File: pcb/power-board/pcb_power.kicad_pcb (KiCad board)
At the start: 2 copper layers, 100 x 79 mm, 25 parts, among them J10 JST_B4B-XH-A, J11 JST_B4P-VH, J12 XT30, K20 FINDER-40.41, K21 FINDER-40.41, Q40 BD249C, Q41 BD139, Q42 BD249C, Q43 BD139

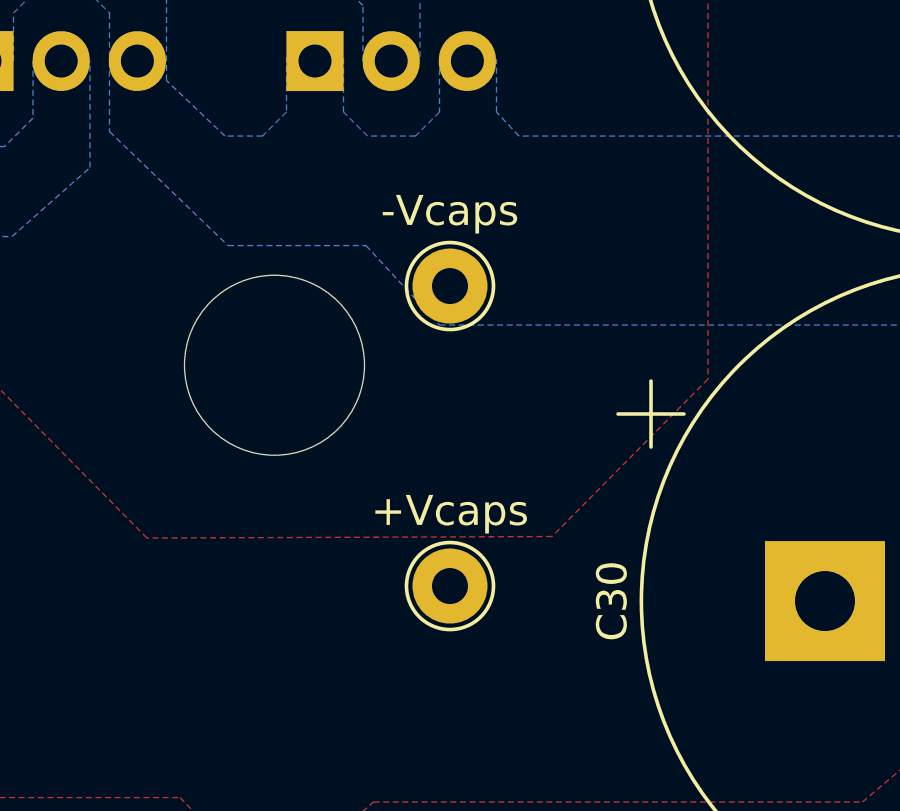
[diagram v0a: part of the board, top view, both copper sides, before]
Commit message: Perform minor stylistic changes on power-board schematic, clear DRC
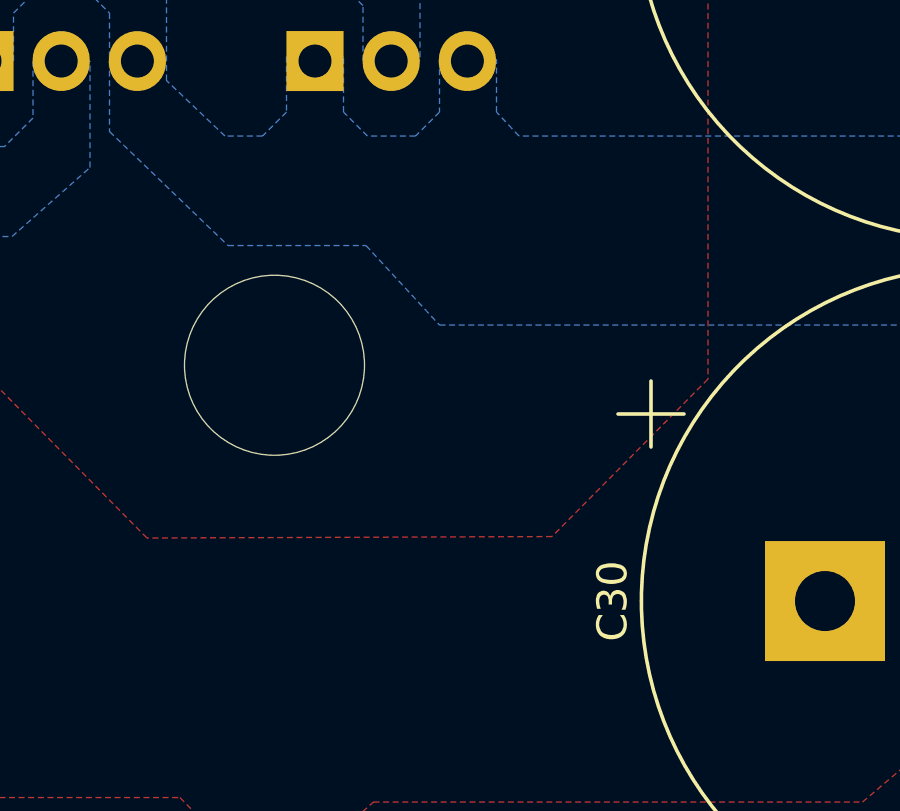
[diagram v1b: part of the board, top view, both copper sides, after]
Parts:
- removed +Vcaps, -Vcaps: TestPoint_THTPad_D2.5mm_Drill1.2mm, TestPoint:TestPoint_THTPad_D2.5mm_Drill1.2mm
- R40, R41: value 220m -> 0R2
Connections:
- net /Power_transistors/base renamed /Series pass transistors/base
- net /Power_transistors/collector renamed /Rectifier/+DC
- net /Power_transistors/emitter renamed /Series pass transistors/emitter
- net /Power_transistors/pwr_e1 renamed /Series pass transistors/pwr_e1
- net /Power_transistors/pwr_e2 renamed /Series pass transistors/pwr_e2
- net /Power_transistors/pwr_eb1 renamed /Series pass transistors/pwr_eb1
- net /Power_transistors/pwr_eb2 renamed /Series pass transistors/pwr_eb2
- net /Tab selector/Relay1 renamed /Tab selector/relay_1
- net /Tab selector/Relay2 renamed /Tab selector/relay_2
- net /Tab selector/Relay_VCC renamed /Tab selector/relay_VCC
